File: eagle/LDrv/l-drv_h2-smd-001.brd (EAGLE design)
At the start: 100 x 80 mm, 26 parts, among them IC2 74AC132D, IC3 74AC132D, IC4 74AC132D

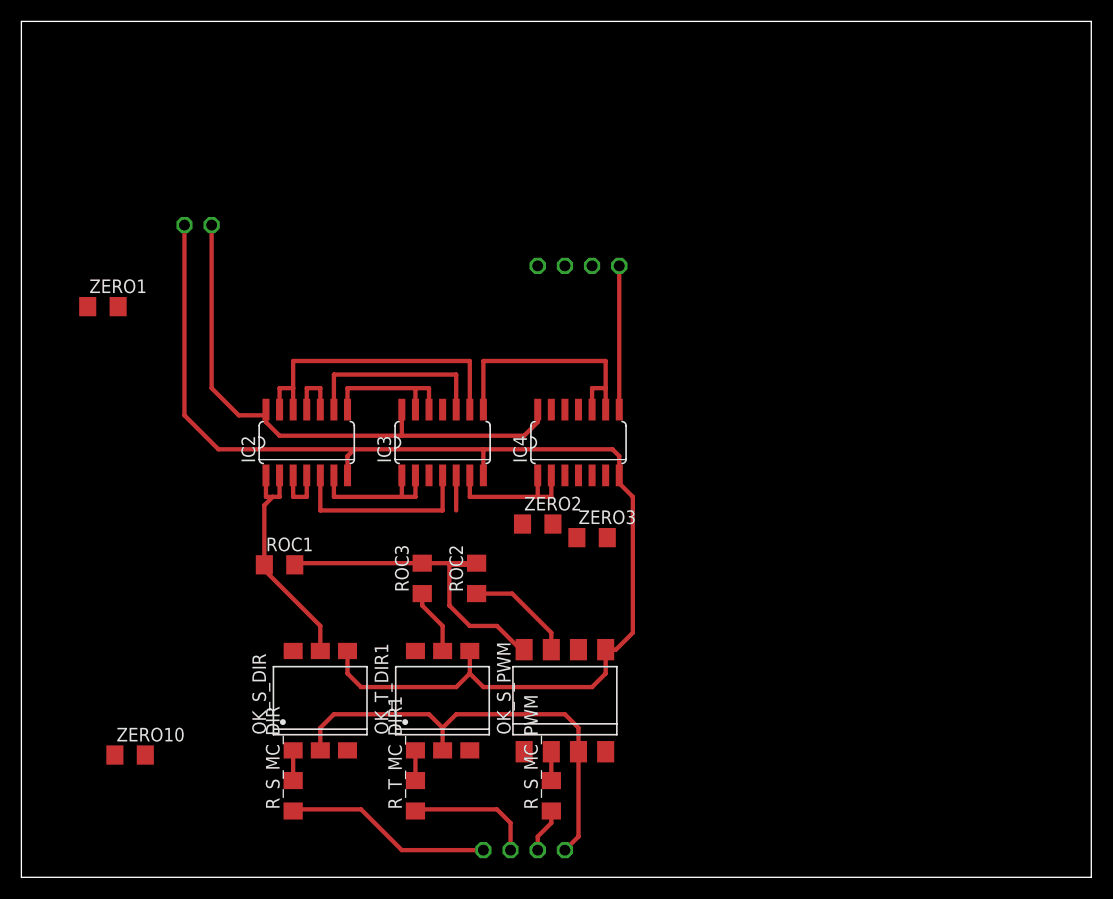
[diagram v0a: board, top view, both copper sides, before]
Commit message: SMD logic circit
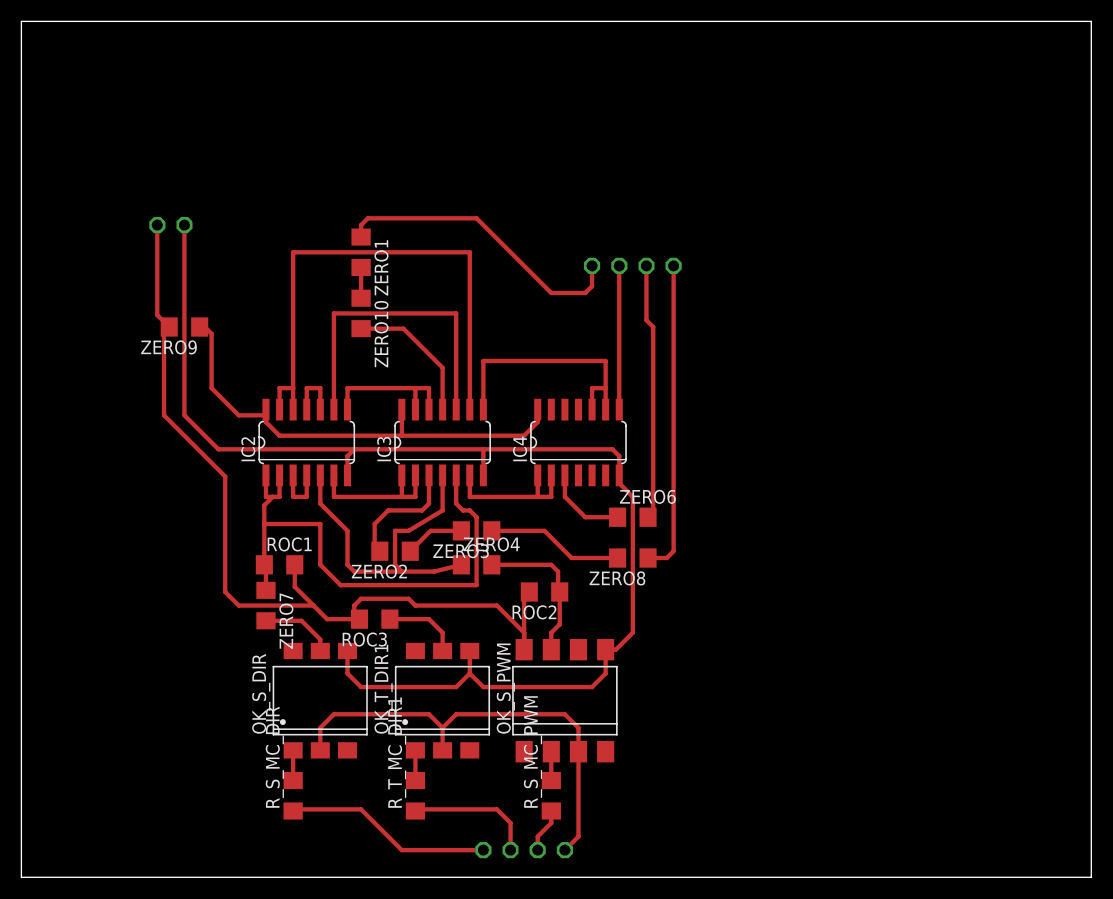
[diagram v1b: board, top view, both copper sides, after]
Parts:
- added ZERO4, ZERO6, ZERO7, ZERO8, ZERO9: (no value), rcl:R1206
- moved ZERO10 46.6 mm to (31.8, 52.7), turned to 270 degrees
- moved ZERO1 24.7 mm to (31.8, 58.4), turned to 270 degrees
- moved ZERO2 13.6 mm to (34.9, 30.5), turned to 180 degrees
- moved JP_H1 12.7 mm to (61.0, 57.1)
- moved ZERO3 10.8 mm to (42.5, 32.4), turned to 180 degrees
- moved JP_L1 7.62 mm to (58.4, 57.1)
- moved ROC2 6.48 mm to (48.9, 26.7), turned to 180 degrees
- moved ROC3 5.85 mm to (33.0, 24.1), turned to 180 degrees
- moved JP6_VCC 5.08 mm to (12.7, 61.0)
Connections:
- new net N$20: OK_S_PWM.7, ROC2.1, ZERO4.2
- new net N$23: JP_L1.1, ZERO6.2
- new net N$24: OK_S_DIR.5, ZERO7.2
- new net N$25: ZERO3.1, ZERO8.2
- new net N$26: JP6_VCC.1, OK_S_PWM.8, ROC1.2, ROC2.2, ROC3.2, ZERO9.2
- net N$14: now also ZERO8.1; no longer ZERO3.1
- net N$17: now also ZERO6.1; no longer JP_L1.1
- net N$D1: now also ZERO7.1; no longer OK_S_DIR.5
- net N$PWM: now also ZERO4.1; no longer OK_S_PWM.7, ROC2.1
- net VCC: now also ZERO9.1; no longer JP6_VCC.1, OK_S_PWM.8, ROC1.2, ROC2.2, ROC3.2
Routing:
- net N$26: track 0.00 -> 81.5 mm
- net VCC: track 84.8 -> 43.8 mm
- net N$14: track 0.00 -> 29.3 mm
- net N$13: track 0.00 -> 28.0 mm
- net N$D1: track 25.5 -> 50.8 mm
- net N$23: track 0.00 -> 24.0 mm
- net N$D2: track 35.0 -> 56.4 mm
- net N$PWM: track 46.0 -> 62.1 mm
- net N$20: track 0.00 -> 14.1 mm
- net N$15: track 0.00 -> 13.0 mm
- net N$25: track 0.00 -> 12.8 mm
- net N$4: track 0.00 -> 11.3 mm
- net N$17: track 0.00 -> 7.72 mm
- net N$24: track 0.00 -> 6.88 mm
- net N$16: track 0.00 -> 5.57 mm
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
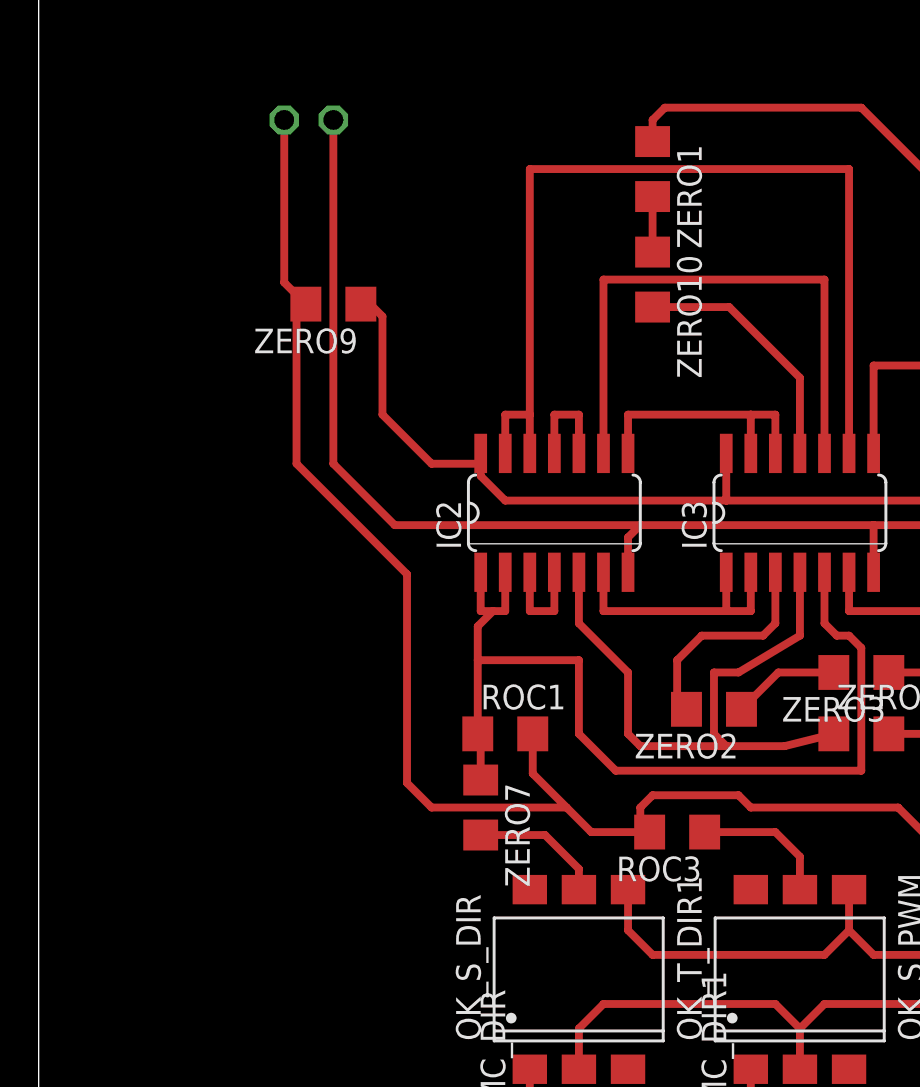
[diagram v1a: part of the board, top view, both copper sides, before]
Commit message: SMD for logic drv
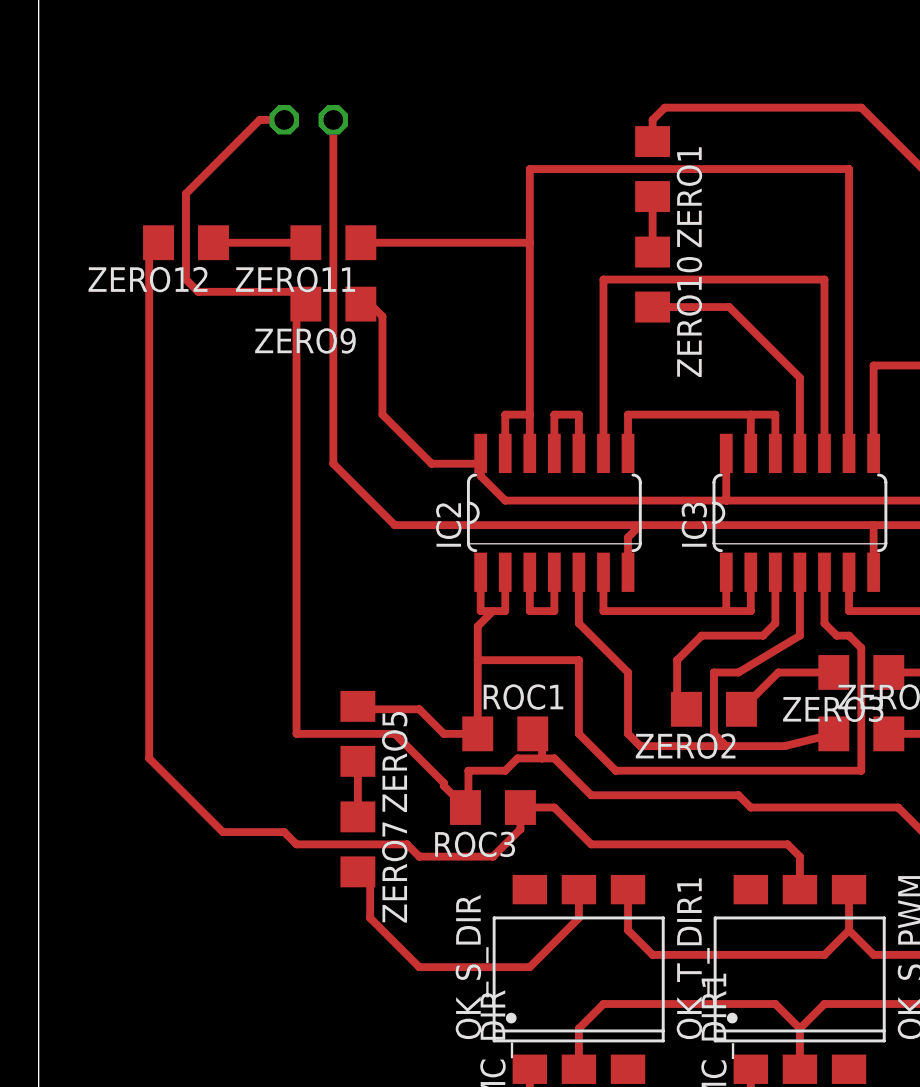
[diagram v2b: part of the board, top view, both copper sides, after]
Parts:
- added ZERO11, ZERO12, ZERO5: (no value), rcl:R1206
- moved ROC3 9.61 mm to (23.5, 25.4)
- moved ZERO7 6.63 mm to (16.5, 23.5)
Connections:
- new net N$22: ZERO5.2, ZERO7.1
- new net N$27: OK_T_DIR1.5, ROC3.1, ZERO12.2
- new net N$28: ZERO11.2, ZERO12.1
- net N$D1: now also ZERO5.1; no longer ZERO7.1
- net N$D2: now also ZERO11.1; no longer OK_T_DIR1.5, ROC3.1
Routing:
- net N$27: track 0.00 -> 67.1 mm
- net N$24: track 6.88 -> 17.0 mm
- net N$26: track 81.5 -> 88.4 mm
- net N$28: track 0.00 -> 4.78 mm
- net N$D1: track 50.8 -> 55.3 mm
- net N$22: track 0.00 -> 2.87 mm
- net N$D2: track 56.4 -> 57.9 mm
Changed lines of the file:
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@@
 <element name="ROC1" library="rcl" package="R1206" value="" x="24.13" y="29.21"/>
 <element name="ROC2" library="rcl" package="R1206" value="" x="48.895" y="26.67" rot="R180"/>
-<element name="ROC3" library="rcl" package="R1206" value="" x="33.02" y="24.13" rot="R180"/>
+<element name="ROC3" library="rcl" package="R1206" value="" x="23.495" y="25.4" rot="R180"/>
 <element name="R_S_MC_DIR" library="rcl" package="R1206" value="" x="25.4" y="7.62" rot="R90"/>
 <element name="R_S_MC_PWM" library="rcl" package="R1206" value="" x="49.53" y="7.62" rot="R90"/>
@@
 <element name="ZERO4" library="rcl" package="R1206" value="" x="42.545" y="29.21"/>
 <element name="ZERO6" library="rcl" package="R1206" value="" x="57.15" y="33.655"/>
-<element name="ZERO7" library="rcl" package="R1206" value="" x="22.86" y="25.4" rot="R270"/>
+<element name="ZERO7" library="rcl" package="R1206" value="" x="16.51" y="23.495" rot="R270"/>
 <element name="ZERO8" library="rcl" package="R1206" value="" x="57.15" y="29.845" rot="R180"/>
 <element name="ZERO9" library="rcl" package="R1206" value="" x="15.24" y="51.435" rot="R180"/>
+<element name="ZERO5" library="rcl" package="R1206" value="" x="16.51" y="29.21" rot="R270"/>
+<element name="ZERO11" library="rcl" package="R1206" value="" x="15.24" y="54.61" rot="R180"/>
+<element name="ZERO12" library="rcl" package="R1206" value="" x="7.62" y="54.61" rot="R180"/>
 </elements>
 <signals>
@@
 </signal>
 <signal name="N$D2">
-<contactref element="OK_T_DIR1" pad="5"/>
-<contactref element="ROC3" pad="1"/>
 <contactref element="IC2" pad="12"/>
 <contactref element="IC2" pad="13"/>
@@
 <wire x1="41.91" y1="43.7134" x2="41.91" y2="58.42" width="0.4064" layer="1"/>
 <wire x1="41.91" y1="58.42" x2="25.4" y2="58.42" width="0.4064" layer="1"/>
-<wire x1="25.4" y1="58.42" x2="25.4" y2="45.72" width="0.4064" layer="1"/>
-<wire x1="39.37" y1="21.155" x2="39.37" y2="22.86" width="0.4064" layer="1"/>
-<wire x1="34.442" y1="24.13" x2="38.1" y2="24.13" width="0.4064" layer="1"/>
-<wire x1="38.1" y1="24.13" x2="39.37" y2="22.86" width="0.4064" layer="1"/>
-<wire x1="38.1" y1="24.13" x2="41.91" y2="43.7134" width="0" layer="19" extent="1-1"/>
+<wire x1="25.4" y1="58.42" x2="25.4" y2="54.61" width="0.4064" layer="1"/>
+<contactref element="ZERO11" pad="1"/>
+<wire x1="25.4" y1="54.61" x2="25.4" y2="45.72" width="0.4064" layer="1"/>
+<wire x1="16.662" y1="54.61" x2="25.4" y2="54.61" width="0.4064" layer="1"/>
 </signal>
 <signal name="N$PWM">
@@
 <wire x1="42.545" y1="33.655" x2="42.545" y2="27.305" width="0.4064" layer="1"/>
 <wire x1="27.94" y1="29.21" x2="29.845" y2="27.305" width="0.4064" layer="1"/>
-<contactref element="ZERO7" pad="1"/>
-<wire x1="22.86" y1="26.822" x2="22.86" y2="29.058" width="0.4064" layer="1"/>
 <wire x1="22.86" y1="29.058" x2="22.708" y2="29.21" width="0.4064" layer="1"/>
+<contactref element="ZERO5" pad="1"/>
+<wire x1="22.708" y1="29.21" x2="20.955" y2="29.21" width="0.4064" layer="1"/>
+<wire x1="20.955" y1="29.21" x2="19.685" y2="30.48" width="0.4064" layer="1"/>
+<wire x1="19.685" y1="30.48" x2="16.662" y2="30.48" width="0.4064" layer="1"/>
+<wire x1="16.662" y1="30.48" x2="16.51" y2="30.632" width="0.4064" layer="1"/>
 </signal>
 <signal name="N$5">
@@
 <contactref element="ZERO7" pad="2"/>
 <contactref element="OK_S_DIR" pad="5"/>
-<wire x1="22.86" y1="23.978" x2="26.187" y2="23.978" width="0.4064" layer="1"/>
-<wire x1="26.187" y1="23.978" x2="27.94" y2="22.225" width="0.4064" layer="1"/>
-<wire x1="27.94" y1="22.225" x2="27.94" y2="21.155" width="0.4064" layer="1"/>
+<wire x1="27.94" y1="21.155" x2="27.94" y2="19.685" width="0.4064" layer="1"/>
+<wire x1="27.94" y1="19.685" x2="25.4" y2="17.145" width="0.4064" layer="1"/>
+<wire x1="25.4" y1="17.145" x2="19.685" y2="17.145" width="0.4064" layer="1"/>
+<wire x1="19.685" y1="17.145" x2="17.145" y2="19.685" width="0.4064" layer="1"/>
+<wire x1="17.145" y1="19.685" x2="17.145" y2="21.438" width="0.4064" layer="1"/>
+<wire x1="17.145" y1="21.438" x2="16.51" y2="22.073" width="0.4064" layer="1"/>
 </signal>
 <signal name="N$25">
@@
 <contactref element="ROC2" pad="2"/>
 <contactref element="ZERO9" pad="2"/>
-<wire x1="25.552" y1="29.21" x2="25.552" y2="27.153" width="0.4064" layer="1"/>
-<wire x1="25.552" y1="27.153" x2="27.305" y2="25.4" width="0.4064" layer="1"/>
-<wire x1="28.575" y1="24.13" x2="31.598" y2="24.13" width="0.4064" layer="1"/>
 <wire x1="46.99" y1="21.28" x2="46.99" y2="26.187" width="0.4064" layer="1"/>
 <wire x1="46.99" y1="26.187" x2="47.473" y2="26.67" width="0.4064" layer="1"/>
@@
 <wire x1="44.45" y1="25.4" x2="36.83" y2="25.4" width="0.4064" layer="1"/>
 <wire x1="36.83" y1="25.4" x2="36.195" y2="26.035" width="0.4064" layer="1"/>
-<wire x1="36.195" y1="26.035" x2="31.75" y2="26.035" width="0.4064" layer="1"/>
-<wire x1="31.75" y1="26.035" x2="31.115" y2="25.4" width="0.4064" layer="1"/>
-<wire x1="31.115" y1="25.4" x2="31.115" y2="24.613" width="0.4064" layer="1"/>
-<wire x1="31.115" y1="24.613" x2="31.598" y2="24.13" width="0.4064" layer="1"/>
-<wire x1="28.575" y1="24.13" x2="27.305" y2="25.4" width="0.4064" layer="1"/>
-<wire x1="27.305" y1="25.4" x2="20.32" y2="25.4" width="0.4064" layer="1"/>
-<wire x1="20.32" y1="25.4" x2="19.05" y2="26.67" width="0.4064" layer="1"/>
-<wire x1="19.05" y1="26.67" x2="19.05" y2="37.465" width="0.4064" layer="1"/>
-<wire x1="19.05" y1="37.465" x2="13.335" y2="43.18" width="0.4064" layer="1"/>
-<wire x1="13.335" y1="43.18" x2="13.335" y2="50.952" width="0.4064" layer="1"/>
+<wire x1="36.195" y1="26.035" x2="28.575" y2="26.035" width="0.4064" layer="1"/>
+<wire x1="18.415" y1="29.21" x2="13.335" y2="29.21" width="0.4064" layer="1"/>
+<wire x1="13.335" y1="29.21" x2="13.335" y2="50.952" width="0.4064" layer="1"/>
 <wire x1="13.335" y1="50.952" x2="13.818" y2="51.435" width="0.4064" layer="1"/>
-<wire x1="12.7" y1="60.96" x2="12.7" y2="52.553" width="0.4064" layer="1"/>
-<wire x1="12.7" y1="52.553" x2="13.818" y2="51.435" width="0.4064" layer="1"/>
+<wire x1="18.415" y1="29.21" x2="20.955" y2="26.67" width="0.4064" layer="1"/>
+<wire x1="28.575" y1="26.035" x2="26.67" y2="27.94" width="0.4064" layer="1"/>
+<wire x1="26.67" y1="27.94" x2="26.035" y2="27.94" width="0.4064" layer="1"/>
+<wire x1="26.035" y1="27.94" x2="26.035" y2="28.727" width="0.4064" layer="1"/>
+<wire x1="26.035" y1="28.727" x2="25.552" y2="29.21" width="0.4064" layer="1"/>
+<wire x1="12.7" y1="60.96" x2="11.43" y2="60.96" width="0.4064" layer="1"/>
+<wire x1="11.43" y1="60.96" x2="7.62" y2="57.15" width="0.4064" layer="1"/>
+<wire x1="7.62" y1="57.15" x2="7.62" y2="52.705" width="0.4064" layer="1"/>
+<wire x1="7.62" y1="52.705" x2="8.255" y2="52.07" width="0.4064" layer="1"/>
+<wire x1="8.255" y1="52.07" x2="13.183" y2="52.07" width="0.4064" layer="1"/>
+<wire x1="13.183" y1="52.07" x2="13.818" y2="51.435" width="0.4064" layer="1"/>
+<wire x1="20.955" y1="26.67" x2="20.955" y2="26.518" width="0.4064" layer="1"/>
+<wire x1="20.955" y1="26.518" x2="22.073" y2="25.4" width="0.4064" layer="1"/>
+<wire x1="26.035" y1="27.94" x2="24.765" y2="27.94" width="0.4064" layer="1"/>
+<wire x1="24.765" y1="27.94" x2="24.13" y2="27.305" width="0.4064" layer="1"/>
+<wire x1="24.13" y1="27.305" x2="22.225" y2="27.305" width="0.4064" layer="1"/>
+<wire x1="22.225" y1="27.305" x2="22.225" y2="25.552" width="0.4064" layer="1"/>
+<wire x1="22.225" y1="25.552" x2="22.073" y2="25.4" width="0.4064" layer="1"/>
+</signal>
+<signal name="N$22">
+<contactref element="ZERO5" pad="2"/>
+<contactref element="ZERO7" pad="1"/>
+<wire x1="16.51" y1="24.917" x2="16.51" y2="27.788" width="0.4064" layer="1"/>
+</signal>
+<signal name="N$27">
+<contactref element="ROC3" pad="1"/>
+<contactref element="OK_T_DIR1" pad="5"/>
+<contactref element="ZERO12" pad="2"/>
+<wire x1="39.37" y1="21.155" x2="39.37" y2="22.86" width="0.4064" layer="1"/>
+<wire x1="39.37" y1="22.86" x2="38.735" y2="23.495" width="0.4064" layer="1"/>
+<wire x1="38.735" y1="23.495" x2="28.575" y2="23.495" width="0.4064" layer="1"/>
+<wire x1="28.575" y1="23.495" x2="26.67" y2="25.4" width="0.4064" layer="1"/>
+<wire x1="26.67" y1="25.4" x2="24.917" y2="25.4" width="0.4064" layer="1"/>
+<wire x1="24.917" y1="25.4" x2="24.917" y2="24.282" width="0.4064" layer="1"/>
+<wire x1="24.917" y1="24.282" x2="23.495" y2="22.86" width="0.4064" layer="1"/>
+<wire x1="23.495" y1="22.86" x2="19.685" y2="22.86" width="0.4064" layer="1"/>
+<wire x1="19.685" y1="22.86" x2="19.05" y2="23.495" width="0.4064" layer="1"/>
+<wire x1="19.05" y1="23.495" x2="13.335" y2="23.495" width="0.4064" layer="1"/>
+<wire x1="13.335" y1="23.495" x2="12.7" y2="24.13" width="0.4064" layer="1"/>
+<wire x1="12.7" y1="24.13" x2="9.525" y2="24.13" width="0.4064" layer="1"/>
+<wire x1="9.525" y1="24.13" x2="5.715" y2="27.94" width="0.4064" layer="1"/>
+<wire x1="5.715" y1="27.94" x2="5.715" y2="54.127" width="0.4064" layer="1"/>
+<wire x1="5.715" y1="54.127" x2="6.198" y2="54.61" width="0.4064" layer="1"/>
+</signal>
+<signal name="N$28">
+<contactref element="ZERO11" pad="2"/>
+<contactref element="ZERO12" pad="1"/>
+<wire x1="9.042" y1="54.61" x2="13.818" y2="54.61" width="0.4064" layer="1"/>
 </signal>
 </signals>
